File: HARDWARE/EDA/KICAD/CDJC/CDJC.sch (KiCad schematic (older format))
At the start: 20 parts

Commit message: CONTROL SWITCHS OK
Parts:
- added D?: FBM, LED_THT:LED_D3.0mm, symbol Device:LED
- added D?: NBM, LED_THT:LED_D3.0mm, symbol Device:LED
- added D?: LBM, LED_THT:LED_D3.0mm, symbol Device:LED
- added D?: ELM, LED_THT:LED_D3.0mm, symbol Device:LED
- added D?: MRLM, LED_THT:LED_D3.0mm, symbol Device:LED
- added R? (x5): 150K, Resistor_THT:R_Axial_DIN0207_L6.3mm_D2.5mm_P7.62mm_Horizontal, symbol Device:R
- added U? (x2): 74LS32, symbol 74xx:74LS32
- added U? (x2): 74LS04, symbol 74xx:74LS04
- added U? (x2): 74LS08, symbol 74xx:74LS08
- D? (x3): footprint (none) -> LED_THT:LED_D3.0mm
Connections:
- net labels added: FBMon, NBMon
- wire segments 66 -> 101
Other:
- note added: "E LOOP MODE(ELM)"
- note added: "FB:0, NB:1, LB:0"
- note added: "FB:1, NB:0, LB:0"
- note added: "First Board MODE(FBM)"
- note added: "LEDS MODE MONITOR"
- note added: "Last Board MODE(LBM)"
- note added: "MR LOOP MODE(MRLM)"
- note added: "Nº Board MODE(NBM)"
- note removed: "E LOOP MODE(ELMout)"
- note removed: "LB MODE(ELMout)"
- note removed: "MR LOOP MODE(MRLMout)"
- moved on the sheet: D?, R?, SW?, U?A, U?B, U?C

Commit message: CONNECTORS OK
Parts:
- added C?: 100nF, Capacitor_THT:C_Rect_L7.0mm_W2.5mm_P5.00mm, symbol Device:C
- added C?: 1800µF 6.3V, Capacitor_THT:CP_Radial_D10.0mm_P5.00mm, symbol Device:CP
- added J?: POWER_OUT, Connector_PinHeader_2.00mm:PinHeader_1x03_P2.00mm_Horizontal, symbol Connector_Generic:Conn_01x03
- added J?: COM_IN, Connector_PinHeader_2.00mm:PinHeader_1x05_P2.00mm_Horizontal, symbol Connector_Generic:Conn_01x05
- added J?: COM_OUT, Connector_PinHeader_2.00mm:PinHeader_1x05_P2.00mm_Horizontal, symbol Connector_Generic:Conn_01x05
- added J?: POWER_IN, Connector_PinHeader_2.00mm:PinHeader_1x03_P2.00mm_Horizontal, symbol Connector_Generic:Conn_01x03
- added U?: 4017, Package_DIP:DIP-16_W7.62mm_LongPads, symbol 4xxx:4017
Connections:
- net labels added: !LBO, CLK, EI, FBO, GNDD, LBLBI, MRI
- net labels removed: GND
- wire segments 101 -> 132
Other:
- note added: "CONNECTORS"

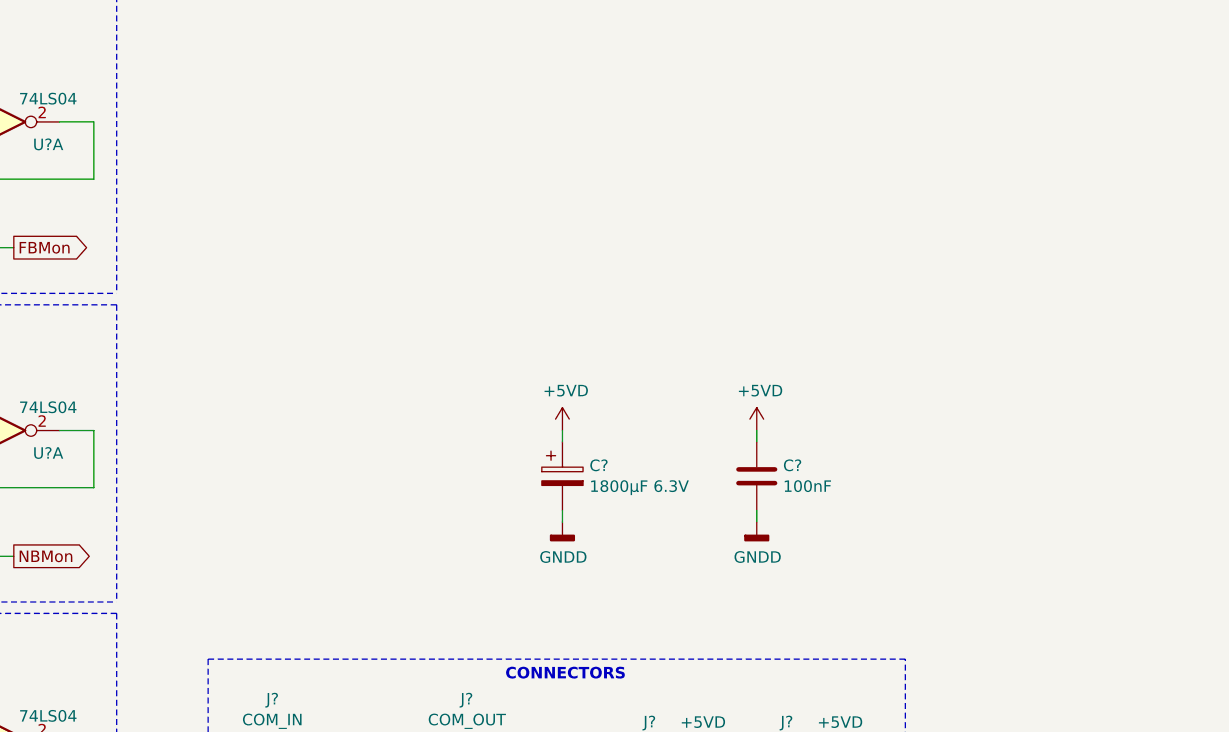
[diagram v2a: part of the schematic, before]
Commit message: capacitor decoupling OK
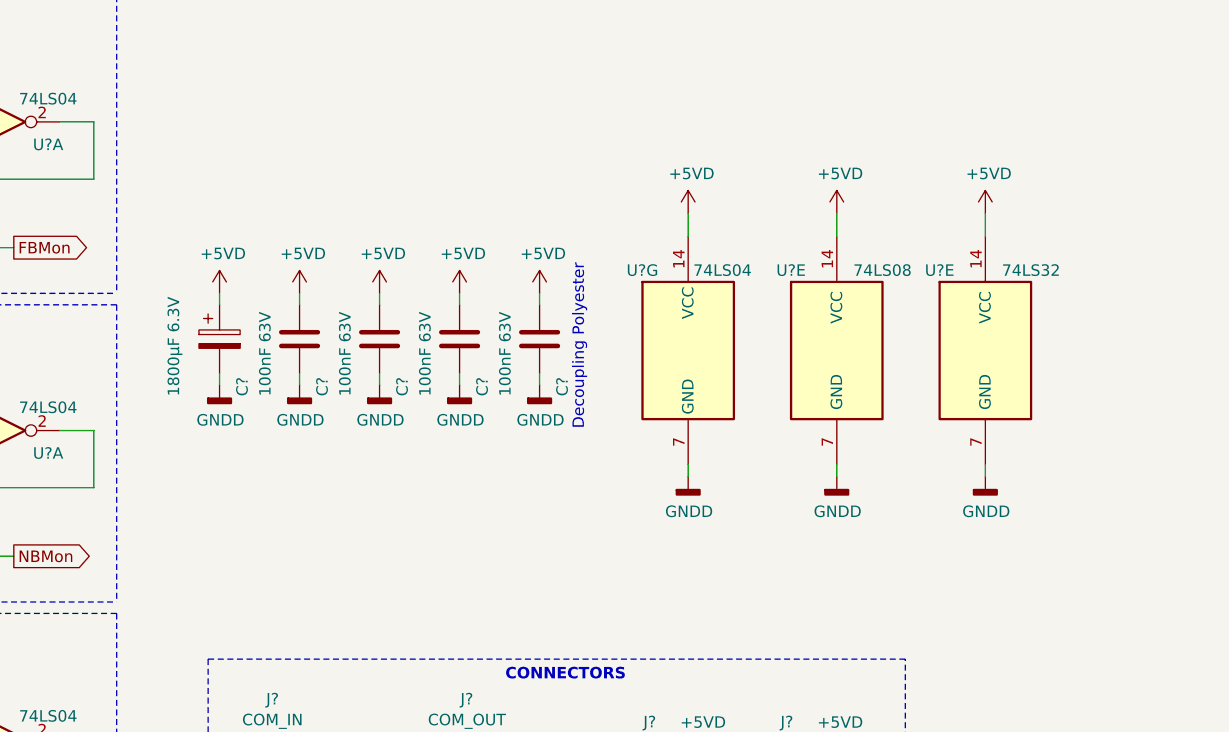
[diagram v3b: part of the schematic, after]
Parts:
- added C? (x3): 100nF 63V, Capacitor_THT:C_Rect_L7.0mm_W2.5mm_P5.00mm, symbol Device:C
- added U?: 74LS04, symbol 74xx:74LS04
- added U?: 74LS08, symbol 74xx:74LS08
- added U?: 74LS32, symbol 74xx:74LS32
- C?: value 100nF -> 100nF 63V
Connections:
- net +5VD: now also C?.1, C?.1, C?.1, U?.14 (VCC), U?.14 (VCC), U?.14 (VCC)
- net GNDD: now also C?.2, C?.2, C?.2, U?.7 (GND), U?.7 (GND), U?.7 (GND)
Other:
- note added: "Decoupling Polyester"
- moved on the sheet: C?

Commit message: OUTPUTS 4017 PK
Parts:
- added C?: 100nF 63V, Capacitor_THT:C_Rect_L7.0mm_W2.5mm_P5.00mm, symbol Device:C
- added D? (x10): 1N4148, Diode_THT:D_DO-35_SOD27_P7.62mm_Horizontal, symbol Diode:1N4148
- added J?: BIT_OUT, Connector_PinHeader_2.00mm:PinHeader_1x08_P2.00mm_Horizontal, symbol Connector_Generic:Conn_01x08
- added U? (x5): 74LS08, symbol 74xx:74LS08
- added U?: 74LS32, symbol 74xx:74LS32
- added U?: 74LS04, symbol 74xx:74LS04
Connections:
- net !LBO: now also U?.6
- net +5VD: now also C?.1, U?.14 (VCC)
- net EB_SW: now also U?.10, U?.13, U?.5; no longer U?.2, U?.5, U?.5
- net FBMon: now also U?.3; no longer U?.6
- net FBO: now also U?.3
- net FB_SW: now also U?.2, U?.4, U?.9, U?.9; no longer U?.1, U?.1, U?.1, U?.5
- net GNDD: now also C?.2, U?.12, U?.12, U?.13, U?.13, U?.7 (GND)
- net LBLBI: now also U?.8
- net LBMon: now also U?.8; no longer U?.6
- net MRLMon: now also U?.11; no longer U?.6
- net NB_SW: now also U?.10, U?.10; no longer U?.2, U?.2
- net at U?.4: now also U?.10; no longer U?.2
- net at U?.3: now also U?.9; no longer U?.1
- net at U?.1 (Q5): now also D?.2 (A)
- net at U?.10 (Q4): now also D?.2 (A)
- net at U?.11 (Q9): now also D?.2 (A)
- net at U?.2 (Q1): now also D?.2 (A)
- net at U?.3 (Q0): now also D?.2 (A)
- net at U?.4 (Q2): now also D?.2 (A)
- net at U?.5 (Q6): now also D?.2 (A)
- net at U?.6 (Q7): now also D?.2 (A)
- net at U?.7 (Q3): now also D?.2 (A)
- net at U?.9 (Q8): now also D?.2 (A)
- new net: U?.12, U?.8
- new net: U?.11, U?.6
- new net: U?.13, U?.8
- new net: U?.12, U?.9
- new net: U?.1, U?.8
- new net: D?.1 (K), U?.3, U?.9
- new net: U?.4, U?.4
- new net: D?.1 (K), U?.2
- new net: D?.1 (K), J?.1 (Pin_1)
- new net: D?.1 (K), J?.2 (Pin_2)
- new net: D?.1 (K), J?.3 (Pin_3)
- new net: D?.1 (K), J?.4 (Pin_4)
- new net: D?.1 (K), J?.5 (Pin_5)
- new net: D?.1 (K), J?.6 (Pin_6)
- new net: D?.1 (K), J?.7 (Pin_7)
- new net: D?.1 (K), J?.8 (Pin_8)
- no-connect marks 0 -> 2
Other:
- moved on the sheet: C?, U?, U?E, U?G
